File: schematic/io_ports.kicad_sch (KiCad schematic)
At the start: 5 parts, among them J1 Cartridge Port, J2 Expansion Port

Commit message: inital change to cpld
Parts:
- removed J2: Expansion Port, Connector_PCBEdge_EXT:Colecovision_Expansion, symbol Connector_Generic:Conn_02x30_Counter_Clockwise
- removed R16: 3K3, Resistor_THT:R_Axial_DIN0207_L6.3mm_D2.5mm_P10.16mm_Horizontal, symbol Device:R
- removed R26: 470R, Resistor_THT:R_Axial_DIN0207_L6.3mm_D2.5mm_P10.16mm_Horizontal, symbol Device:R
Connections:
- no-connect marks 2 -> 0

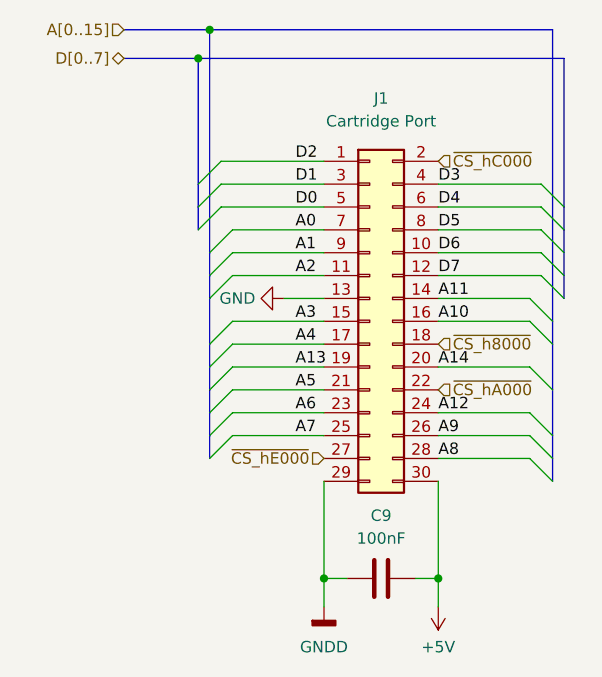
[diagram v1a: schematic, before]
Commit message: first commit of portable coleco, major changes... pcb meh. CPLD code tested, quartus build works.
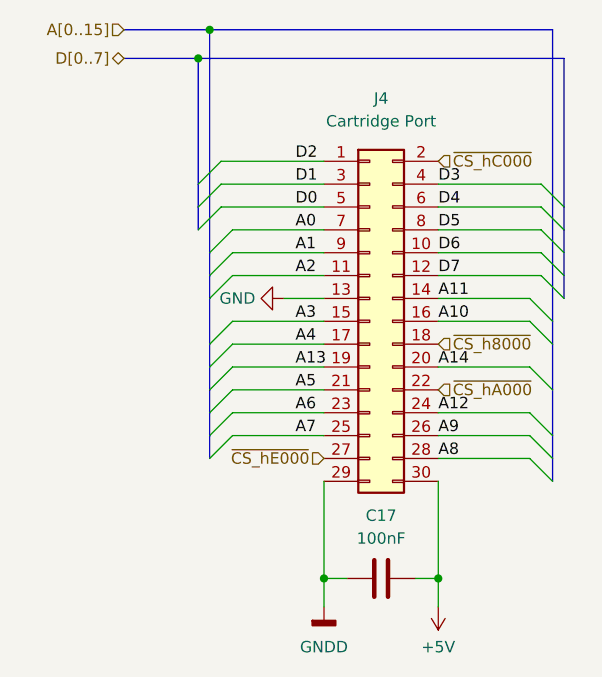
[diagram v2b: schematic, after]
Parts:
- renumbered C9 to C17, J1 to J4
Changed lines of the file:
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@@
   (symbol (lib_id "Connector_Generic:Conn_02x15_Odd_Even") (at 105.41 76.835 0) (unit 1)
     (in_bom yes) (on_board yes) (dnp no) (fields_autoplaced)
-    (property "Reference" "J1" (at 106.68 52.07 0)
+    (property "Reference" "J4" (at 106.68 52.07 0)
       (effects (font (size 1.27 1.27)))
     )
@@
       (project "coleco_original"
         (path "/970e0f64-111f-41e3-9f5a-fb0d0f6fa101/e4e06c1d-a786-4d3d-bc60-24b1ad1e3a25"
-          (reference "J1") (unit 1)
+          (reference "J4") (unit 1)
         )
       )
@@
   (symbol (lib_id "Device:C") (at 106.68 105.41 270) (unit 1)
     (in_bom yes) (on_board yes) (dnp no) (fields_autoplaced)
-    (property "Reference" "C9" (at 106.68 98.425 90)
+    (property "Reference" "C17" (at 106.68 98.425 90)
       (effects (font (size 1.27 1.27)))
     )
@@
       (project "coleco_original"
         (path "/970e0f64-111f-41e3-9f5a-fb0d0f6fa101/e4e06c1d-a786-4d3d-bc60-24b1ad1e3a25"
-          (reference "C9") (unit 1)
+          (reference "C17") (unit 1)
         )
       )
@@
   (symbol (lib_id "power:+5V") (at 113.03 108.585 180) (unit 1)
     (in_bom yes) (on_board yes) (dnp no) (fields_autoplaced)
-    (property "Reference" "#PWR0200" (at 113.03 104.775 0)
+    (property "Reference" "#PWR051" (at 113.03 104.775 0)
       (effects (font (size 1.27 1.27)) hide)
     )
@@
       (project "coleco_original"
         (path "/970e0f64-111f-41e3-9f5a-fb0d0f6fa101/e4e06c1d-a786-4d3d-bc60-24b1ad1e3a25"
-          (reference "#PWR0200") (unit 1)
+          (reference "#PWR051") (unit 1)
         )
       )
@@
   (symbol (lib_id "power:GND") (at 95.885 74.295 270) (unit 1)
     (in_bom yes) (on_board yes) (dnp no)
-    (property "Reference" "#PWR0198" (at 89.535 74.295 0)
+    (property "Reference" "#PWR049" (at 89.535 74.295 0)
       (effects (font (size 1.27 1.27)) hide)
     )
@@
       (project "coleco_original"
         (path "/970e0f64-111f-41e3-9f5a-fb0d0f6fa101/e4e06c1d-a786-4d3d-bc60-24b1ad1e3a25"
-          (reference "#PWR0198") (unit 1)
+          (reference "#PWR049") (unit 1)
         )
       )
@@
   (symbol (lib_id "power:GNDD") (at 100.33 108.585 0) (unit 1)
     (in_bom yes) (on_board yes) (dnp no) (fields_autoplaced)
-    (property "Reference" "#PWR0199" (at 100.33 114.935 0)
+    (property "Reference" "#PWR050" (at 100.33 114.935 0)
       (effects (font (size 1.27 1.27)) hide)
     )
@@
       (project "coleco_original"
         (path "/970e0f64-111f-41e3-9f5a-fb0d0f6fa101/e4e06c1d-a786-4d3d-bc60-24b1ad1e3a25"
-          (reference "#PWR0199") (unit 1)
+          (reference "#PWR050") (unit 1)
         )
       )

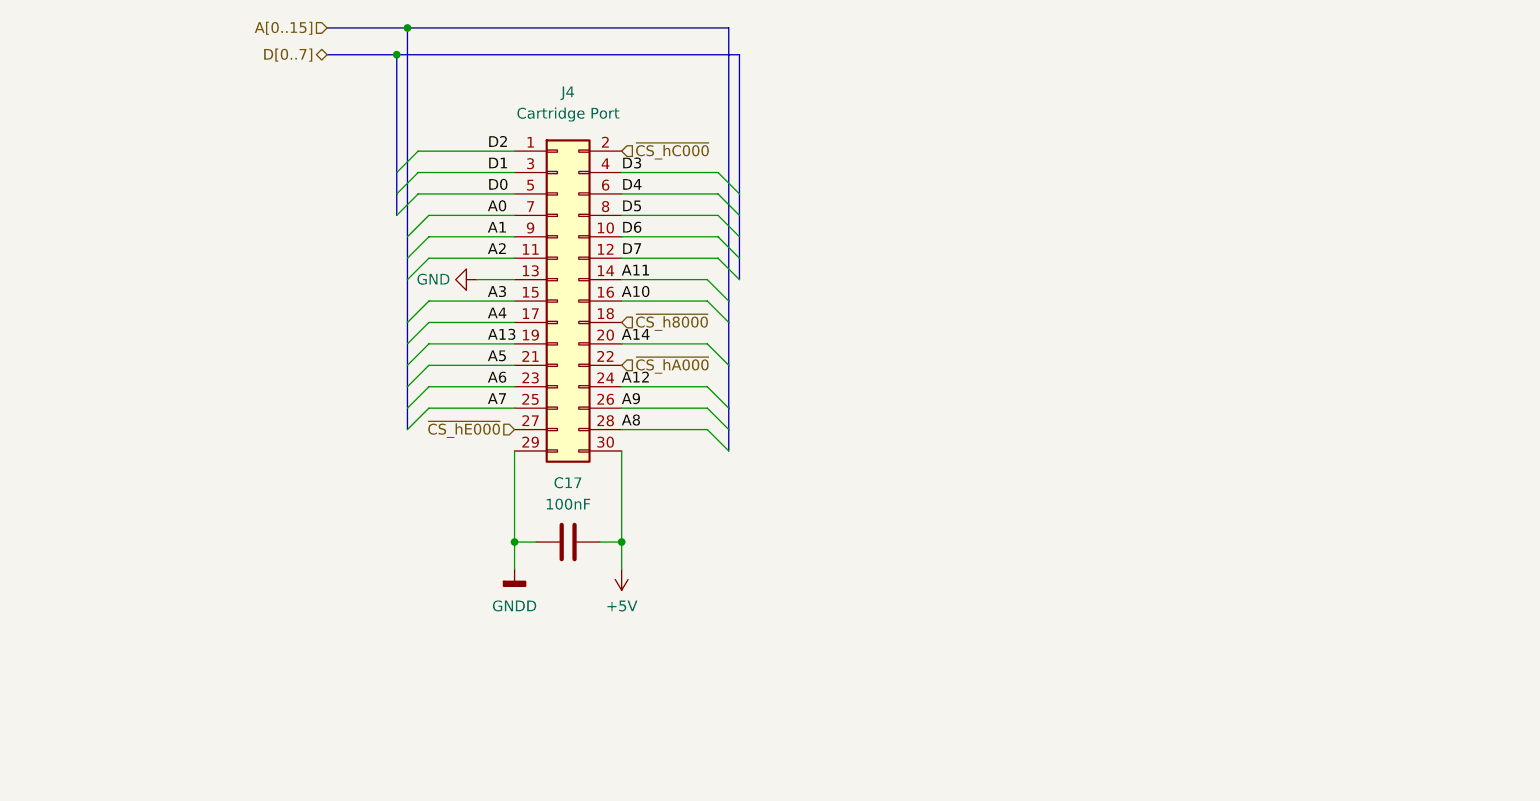
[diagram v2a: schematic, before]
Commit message: added power port for lcd and adjusted board traces and fill
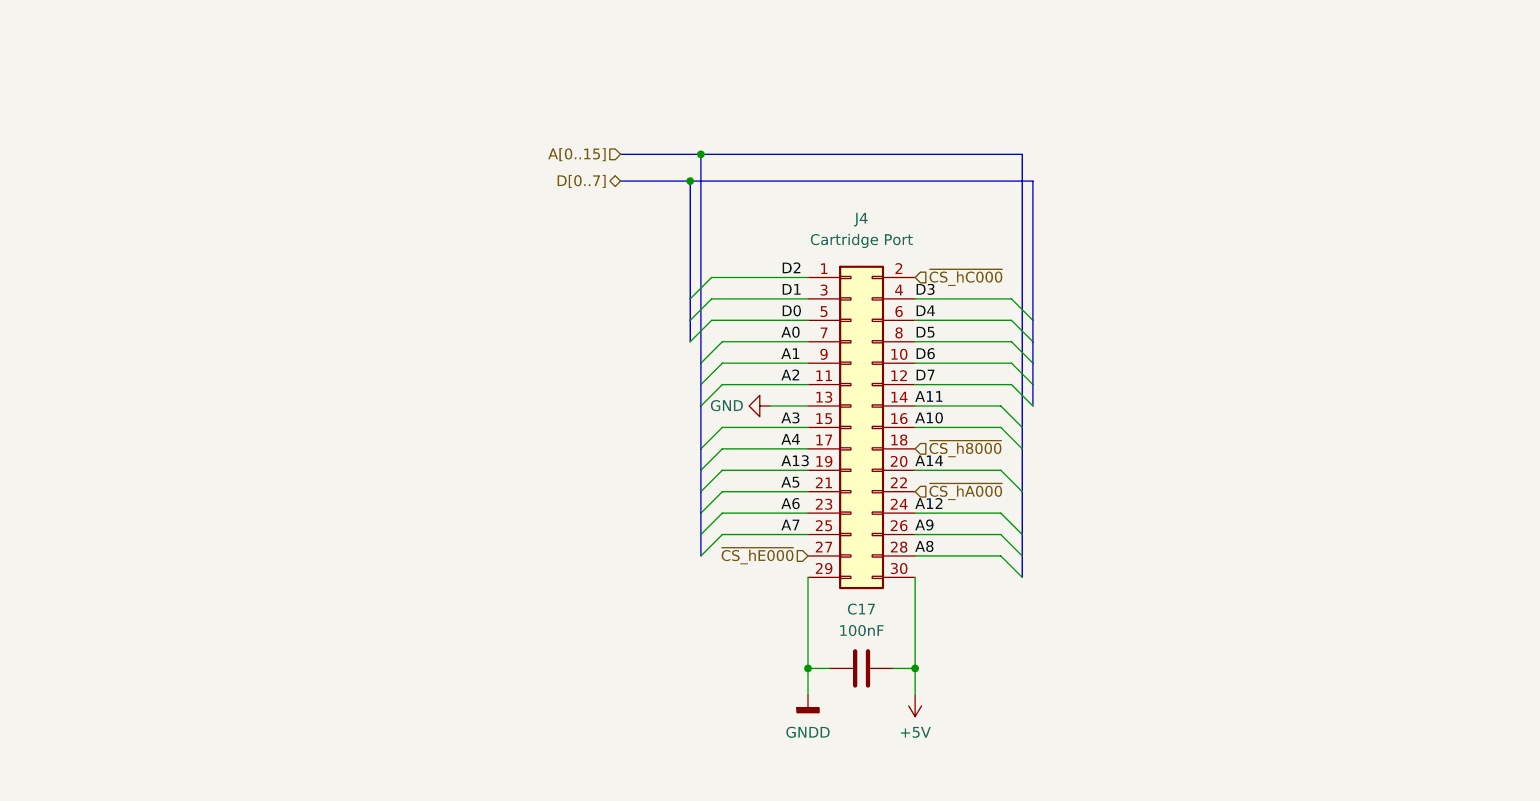
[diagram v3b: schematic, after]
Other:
- moved on the sheet: C17, J4

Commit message: update pdf schematic and schematic wording
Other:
- title: Righteous Tentacle, Colecovision Reverse Engineering Project -> Mini Colecovision
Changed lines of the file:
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@@
   (paper "USLetter")
   (title_block
-    (title "Righteous Tentacle, Colecovision Reverse Engineering Project")
-    (date "2023-06-18")
-    (rev "1.0.0.F")
+    (title "Mini Colecovision")
+    (date "2024-03-25")
+    (rev "1.0.0")
     (company "sparkletron")
     (comment 1 "Jay Convertino")
     (comment 2 "MIT LICENSE")
-    (comment 3 "PCB: 75743 REV F")
+    (comment 3 "TARGET: Portable")
   )
   (junction (at 147.828 120.396) (diameter 0) (color 0 0 0 0)

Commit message: first commit with PCB revised for super game module. Needs model updates and tweaks
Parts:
- C17: footprint Capacitor_THT:C_Disc_D7.0mm_W2.5mm_P5.00mm -> Capacitor_SMD:C_1206_3216Metric
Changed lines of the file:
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@@
       (effects (font (size 1.27 1.27)))
     )
-    (property "Footprint" "Capacitor_THT:C_Disc_D7.0mm_W2.5mm_P5.00mm" (at 137.668 121.3612 0)
+    (property "Footprint" "Capacitor_SMD:C_1206_3216Metric" (at 137.668 121.3612 0)
       (effects (font (size 1.27 1.27)) hide)
     )

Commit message: update for release, correct documents, and update readme
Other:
- moved on the sheet: C17, J4
